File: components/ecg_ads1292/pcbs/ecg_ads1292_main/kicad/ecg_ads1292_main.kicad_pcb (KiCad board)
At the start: 2 copper layers, 65 x 36 mm, 47 parts, among them IC1 ADS1292, J1 Conn_02x04_Odd_Even, P1 Conn_02x20_Odd_Even, U1 TPS73033DBVT

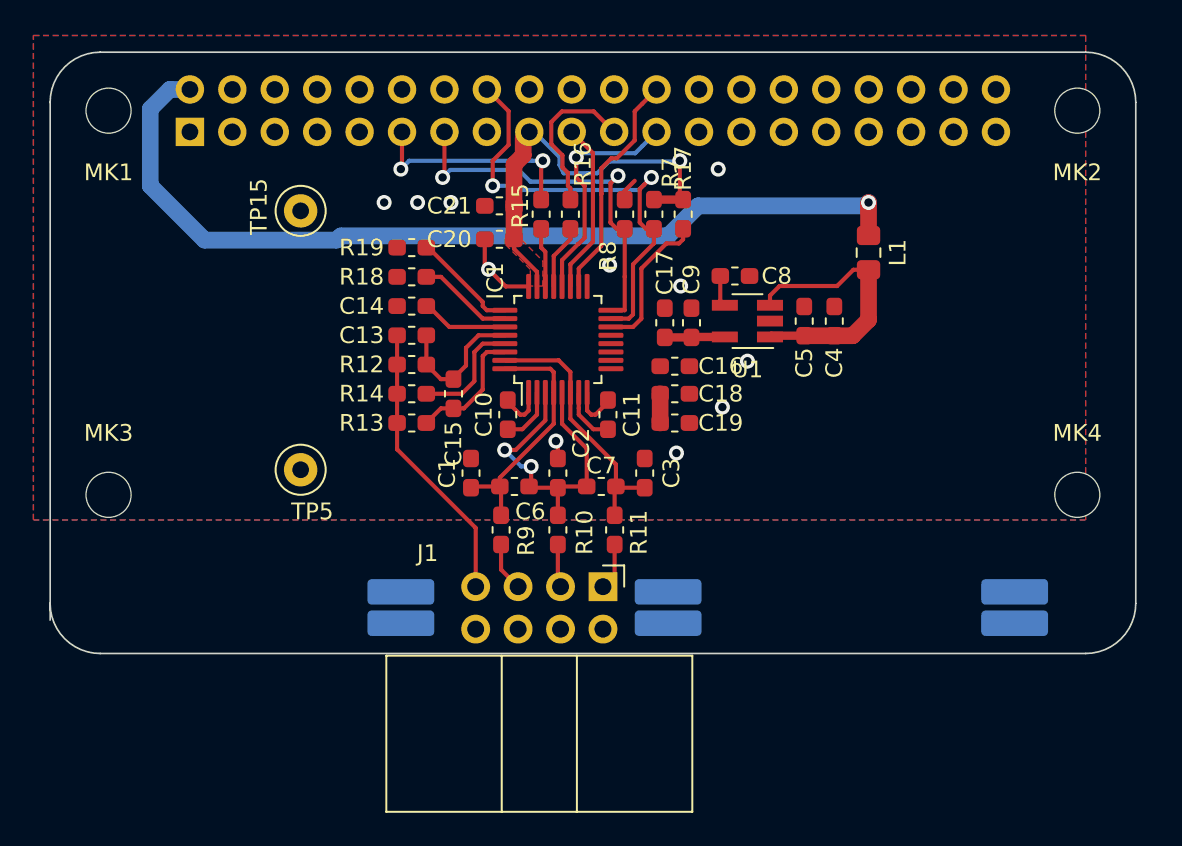
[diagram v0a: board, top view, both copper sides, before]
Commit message: the layout passes the checklist
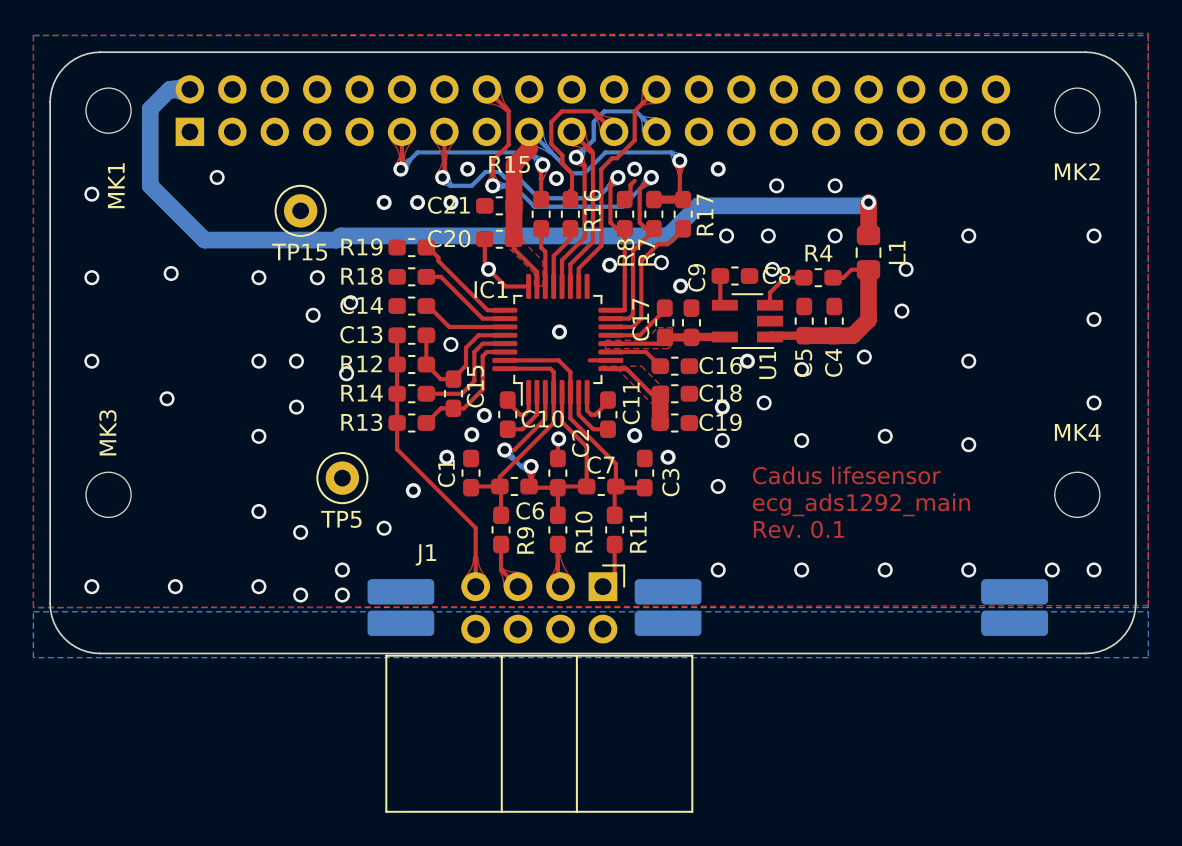
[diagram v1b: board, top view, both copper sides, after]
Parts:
- added R4: 100, Resistor_SMD:R_0603_1608Metric_Pad1.05x0.95mm_HandSolder, F.Cu at (246.0, 107.5)
- moved TP5 2.55 mm to (217.5, 119.5)
- turned TP15 to 180 degrees
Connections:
- U1 pad 3: Net-(C4-Pad1) -> Net-(R4-Pad1)
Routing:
- net GND: track 7.18 -> 12.7 mm, vias 11 -> 73
- net Net-(C4-Pad1): track 16.6 -> 11.8 mm
- net Net-(C18-Pad1): track 1.75 -> 5.31 mm
- net /ECG_Sensor/3.3VA: track 3.61 -> 6.99 mm
- net Net-(C16-Pad1): track 0.00 -> 3.30 mm
- net Net-(R4-Pad1): track 0.00 -> 3.15 mm
- net /SENS_SCLK: track 13.9 -> 15.6 mm
- net /SENS_START: track 23.7 -> 24.7 mm
- net /~SENS_RST_ECG: track 27.7 -> 28.5 mm
- added copper zone on F.Cu, net /ECG_Sensor/3.3VA
- added copper zone on B.Cu, net GNDPWR
- added copper zone on F.Cu, net Net-(C18-Pad1)
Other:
- outline, holes or cut-outs redrawn
- net class Default: clearance 0.25 -> 0.2
- rule trace_clearance: 0.25 -> 0.2
- board text added: "Cadus lifesensor ecg_ads1292_main Rev. 0.1"
- board text removed: "RASPBERRY-PI 40-PIN ADDON BOARD VIEW FROM TOP NOTE: P1 SHOULD BE FITTED ON THE REVERSE OF THE BOARD NOTE: remove pcb edge below MK3/MK4 or MK5/MK6 depending on the board size you need."

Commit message: add board svg image
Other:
- board text removed: "All connectors except the 40 pin header must be angled and must be placed on this edge pointing downwards."
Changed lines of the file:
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@@
   (general
     (thickness 1.6)
-    (drawings 17)
+    (drawings 16)
     (tracks 342)
     (zones 0)
@@
     (arrow2b (pts (xy 200 84) (xy 201.126504 83.413579)))
   )
-  (gr_text "All connectors except the 40 pin header must be angled\nand must be placed on this edge pointing downwards." (at 200 158) (layer Dwgs.User)
-    (effects (font (size 2 1.7) (thickness 0.12)) (justify left))
-  )
   (gr_arc (start 203 127) (end 200 127) (angle -90) (layer Edge.Cuts) (width 0.1))

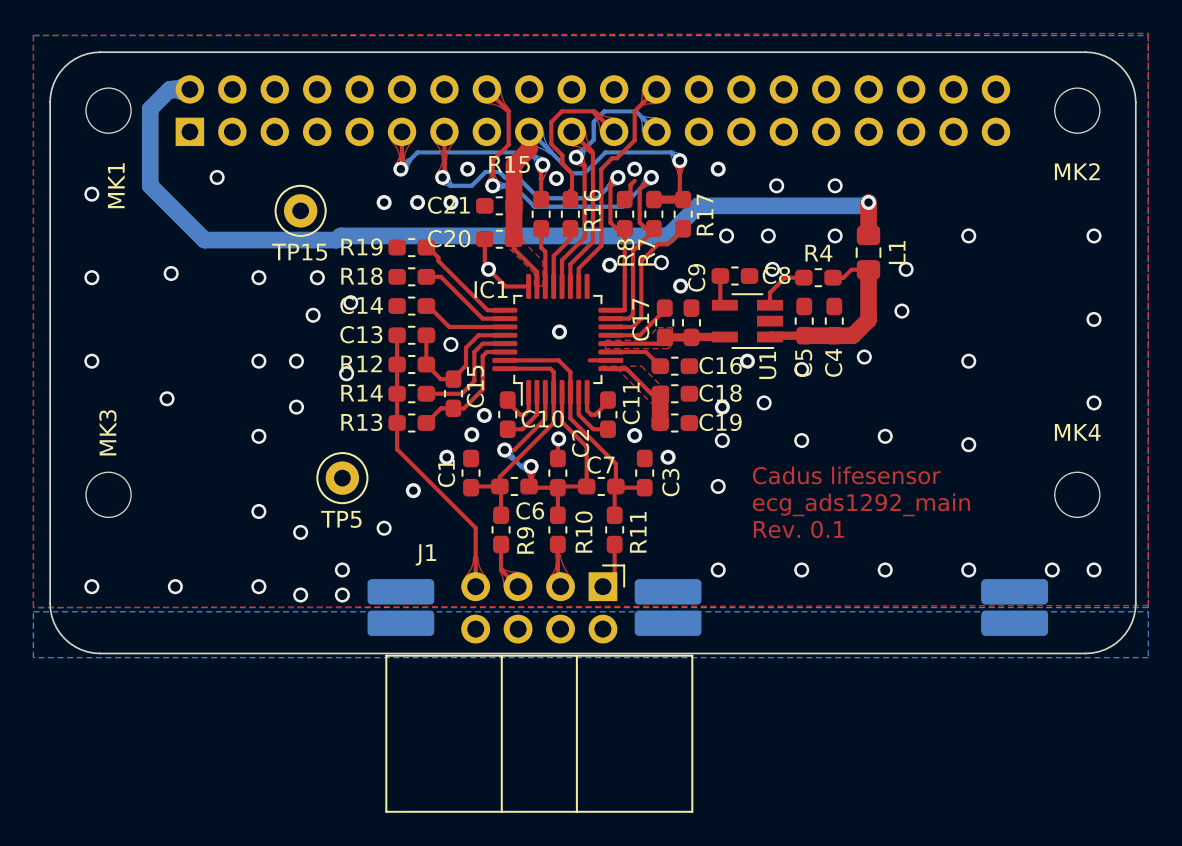
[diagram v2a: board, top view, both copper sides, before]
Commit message: add chip select mux on ads1292_main pcb
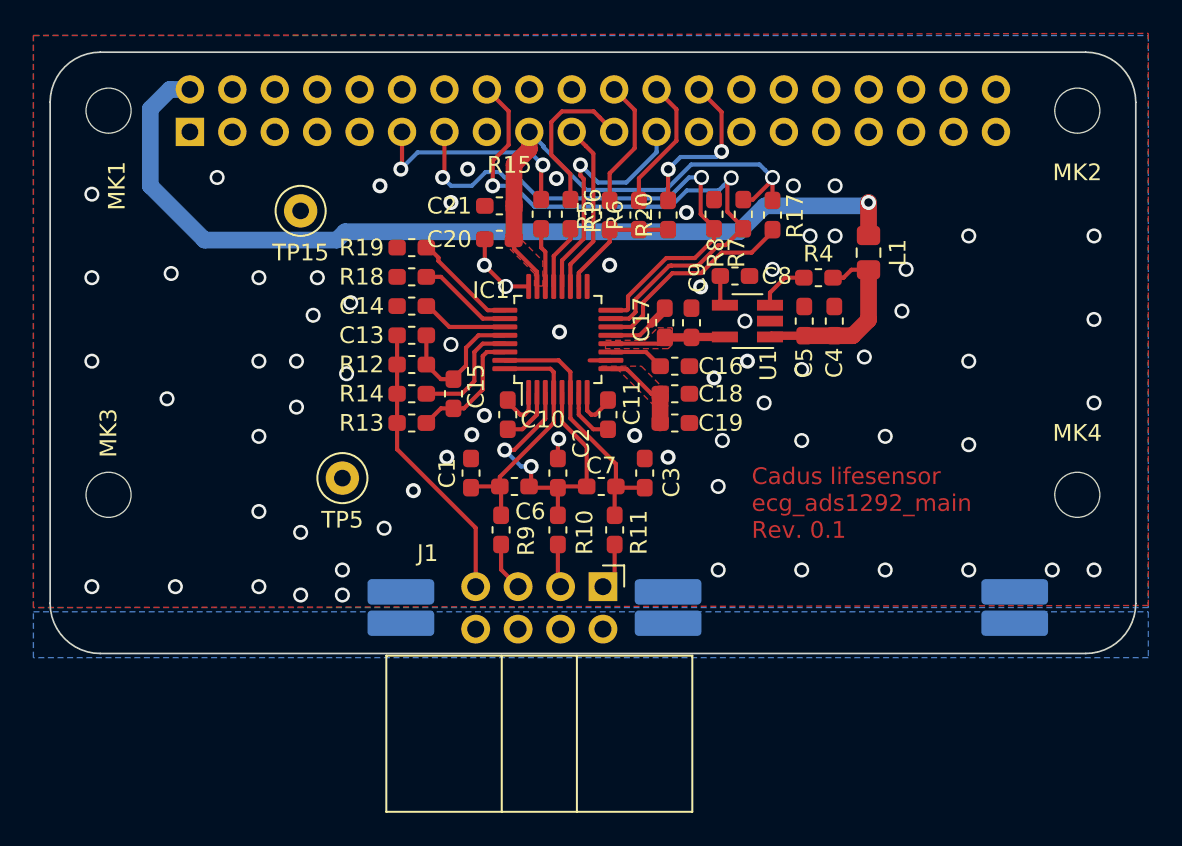
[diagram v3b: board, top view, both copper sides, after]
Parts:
- added R20: 100, Resistor_SMD:R_0603_1608Metric_Pad1.05x0.95mm_HandSolder, F.Cu at (237.0, 103.8)
- added R5: 100, Resistor_SMD:R_0603_1608Metric_Pad1.05x0.95mm_HandSolder, F.Cu at (233.5, 103.8)
- added R6: 100, Resistor_SMD:R_0603_1608Metric_Pad1.05x0.95mm_HandSolder, F.Cu at (235.2, 103.8)
- moved R17 5.35 mm to (243.2, 103.8)
- moved R7 5.35 mm to (241.5, 103.7)
- moved R8 5.35 mm to (239.8, 103.7)
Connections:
- IC1 pad 18: /~SENS_CS_ECG -> /~CS
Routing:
- net /~SENS_CS_SPO2: track 0.00 -> 9.78 mm, vias 0 -> 2
- net /~SENS_RST_ECG: track 28.5 -> 36.4 mm
- net /~SENS_CS_BPM: track 0.00 -> 7.78 mm
- net /SENS_START: track 24.7 -> 32.4 mm
- net /~CS: track 0.00 -> 7.67 mm
- net /~SENS_CS_ECG: track 14.2 -> 8.07 mm
- net +3V3: track 25.1 -> 31.0 mm
- net Net-(IC1-Pad14): track 8.78 -> 12.6 mm
- net GND: track 12.7 -> 11.4 mm, vias 73 -> 71
- net /SENS_SCLK: track 15.6 -> 14.9 mm

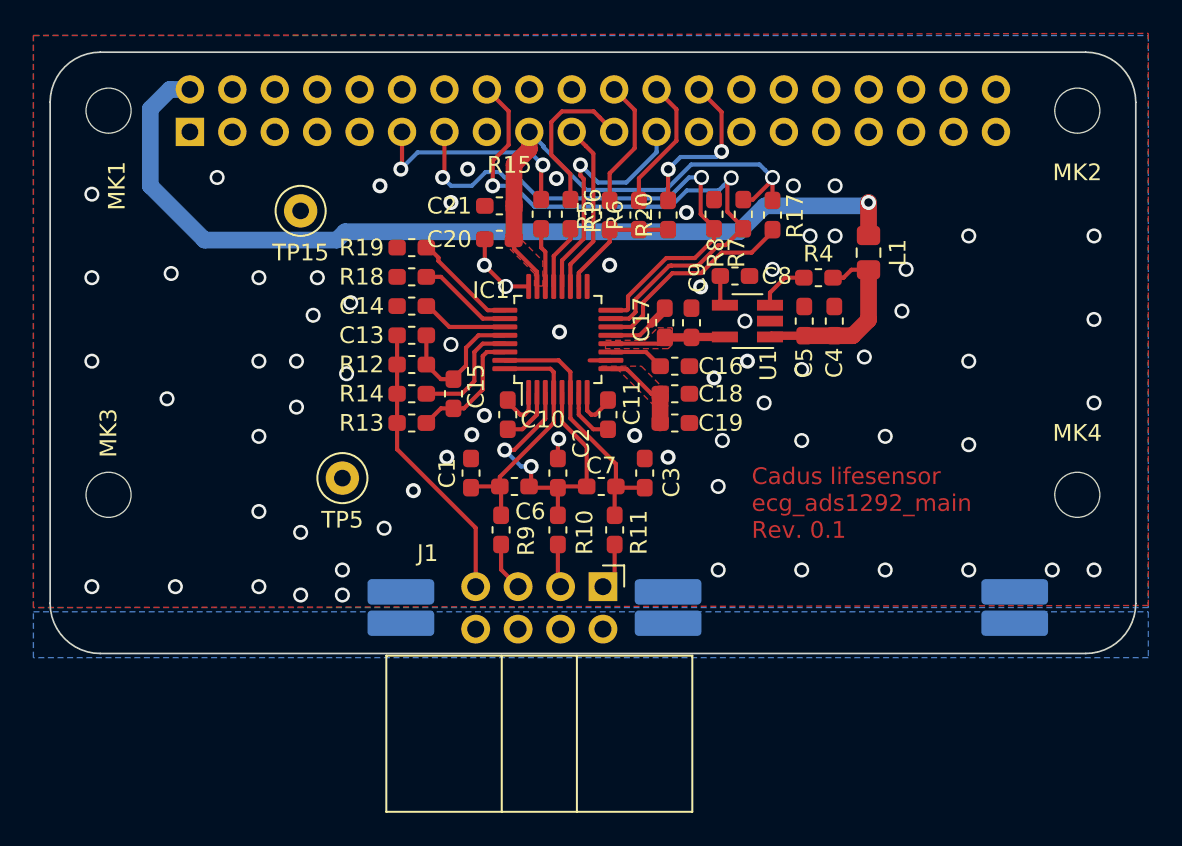
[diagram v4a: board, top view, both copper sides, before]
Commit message: add teardrops to layout
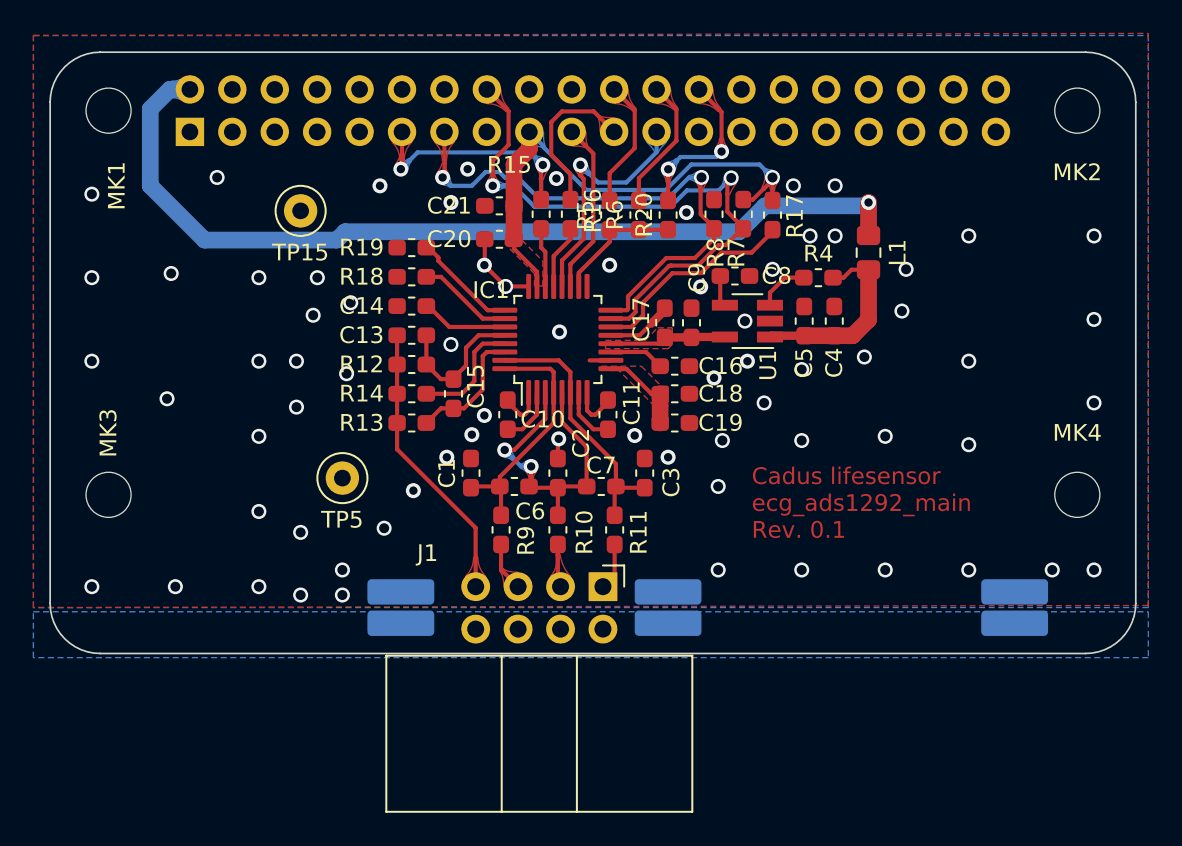
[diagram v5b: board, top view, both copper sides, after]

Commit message: ecg_ads1292 improve input filter circuit
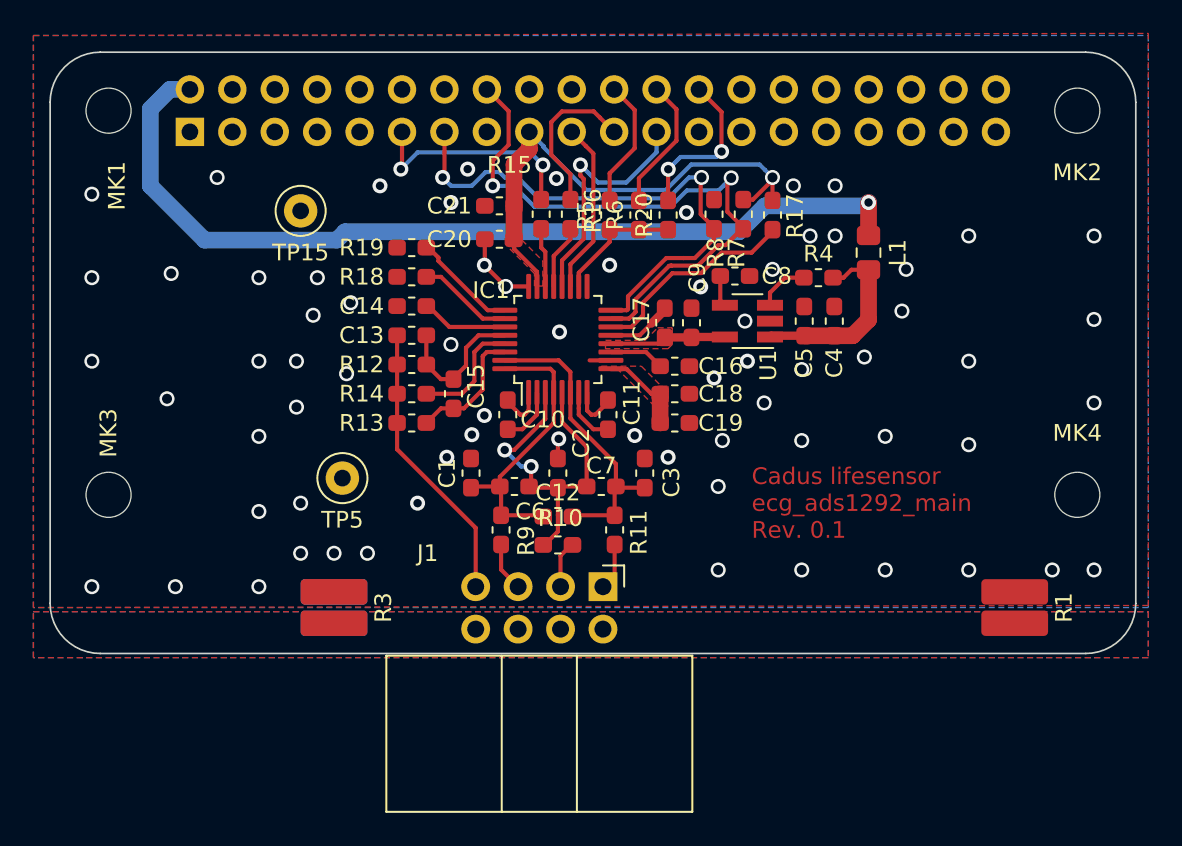
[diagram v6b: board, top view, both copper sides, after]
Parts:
- added C12: n.p., Capacitor_SMD:C_0603_1608Metric_Pad1.05x0.95mm_HandSolder, F.Cu at (230.4, 121.8)
- C1, C2, C3: value 3n -> 47p C0G 50V
- R1, R3: moved to F.Cu
- moved R2 20.0 mm to (217.0, 127.2)
- moved R3 4.00 mm to (217.0, 127.2)
- moved R10 0.90 mm to (230.4, 123.5), turned to 180 degrees
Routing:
- net /ECG_Sensor/ads_in2_p: track 15.7 -> 18.3 mm
- net /ECG_Sensor/ads_in1_p: track 14.7 -> 17.3 mm
- net /ECG_Sensor/ads_in1_n: track 19.9 -> 22.1 mm
- net GND: vias 71 -> 70
- added copper zone on F.Cu, net GNDPWR

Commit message: add teardrops to layout
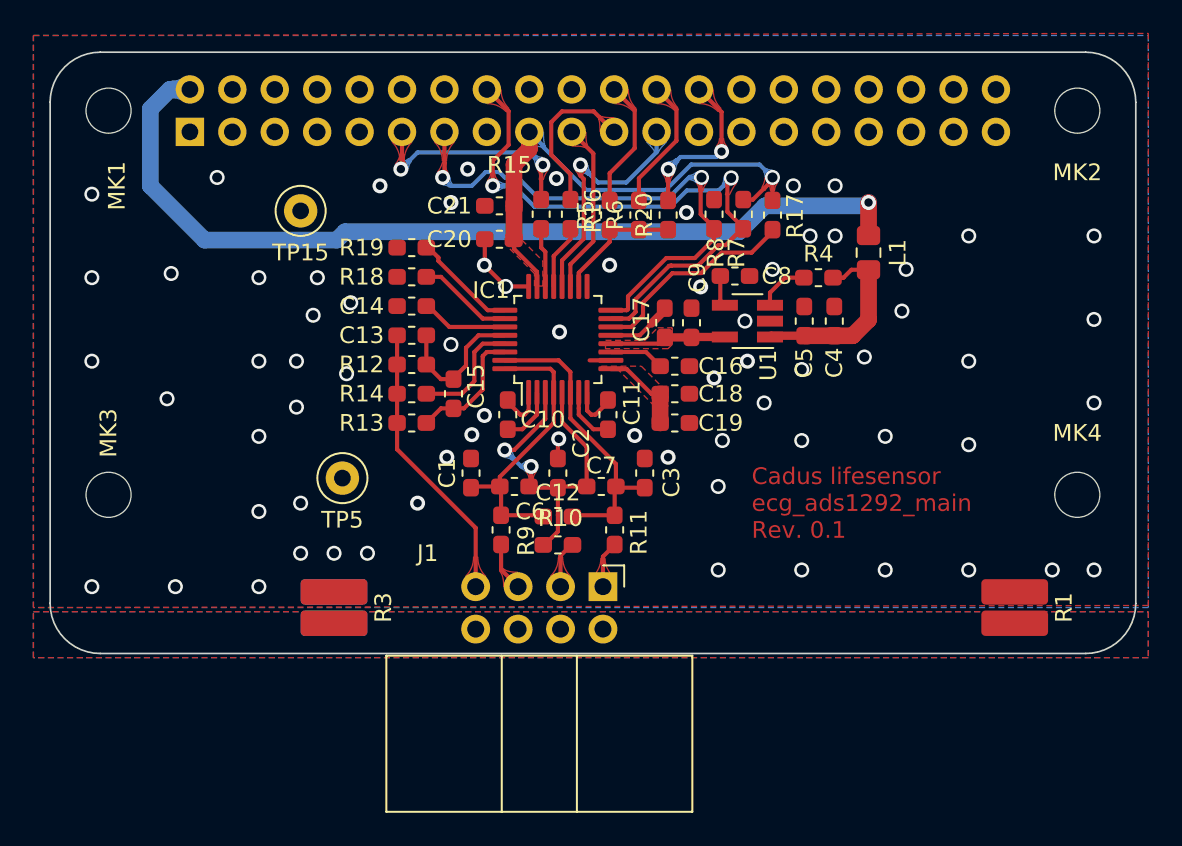
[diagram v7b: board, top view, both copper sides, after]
